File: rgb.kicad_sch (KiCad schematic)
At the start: 4 parts, among them J3 rgb, U3 TPS22916BYFPT

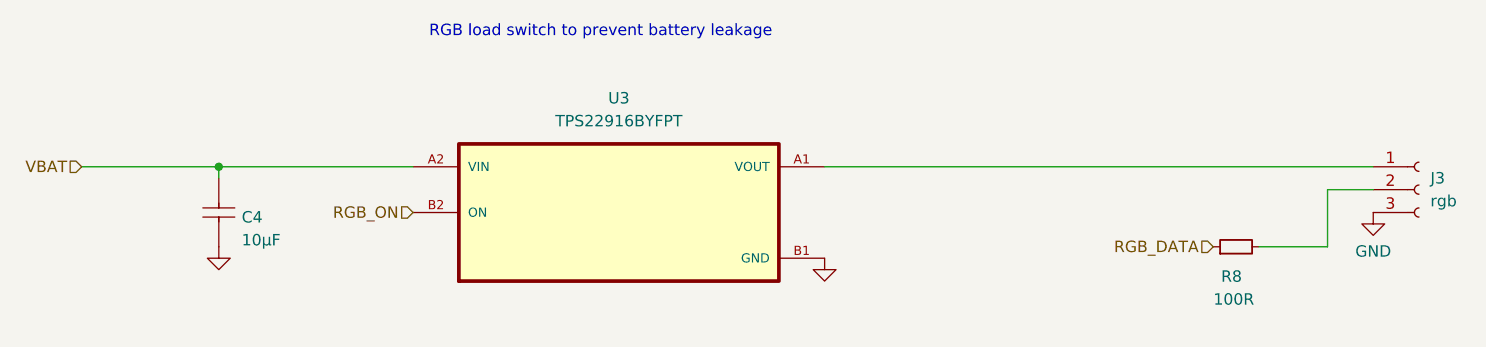
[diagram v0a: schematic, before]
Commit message: Swapping the load switches from WLSP to WSON-6 packages
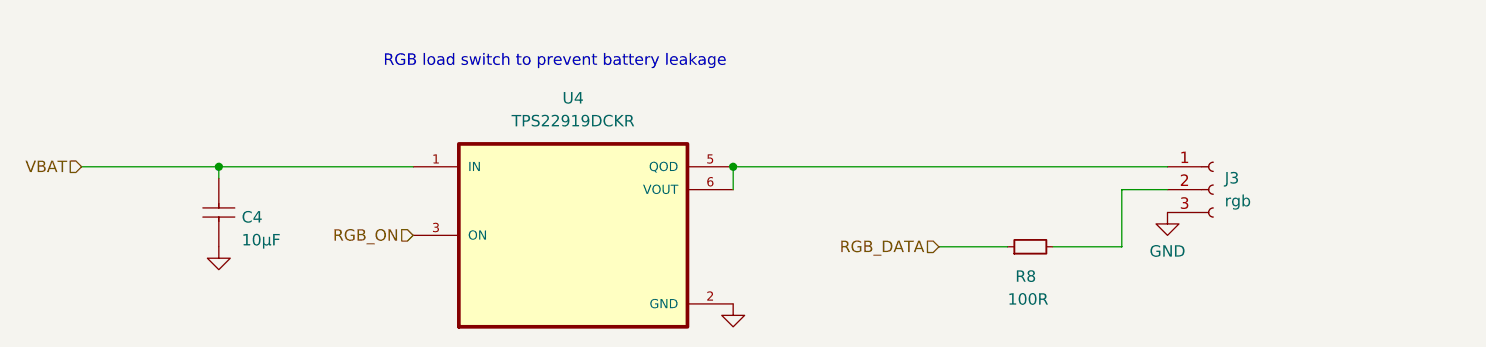
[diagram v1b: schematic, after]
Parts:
- removed U3: TPS22916BYFPT, TPS22916 load switch:BGA4C40P2X2_77X77X50, symbol TPS22916 load switch:TPS22916BYFPT
- added U4: TPS22919DCKR, TPS22919:SOT65P210X110-6N, symbol TPS22919:TPS22919DCKR
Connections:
- net GND: now also U4.2 (GND)
- net RGB_ON: now also U4.3 (ON)
- net VBAT: now also U4.1 (IN)
- net at J3.1 (Pin_1): now also U4.5 (QOD), U4.6 (VOUT)
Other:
- moved on the sheet: J3, R8

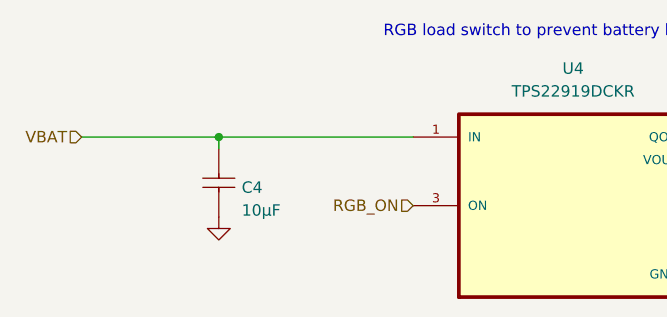
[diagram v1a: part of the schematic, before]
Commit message: Relinking the schematics and the PCB again
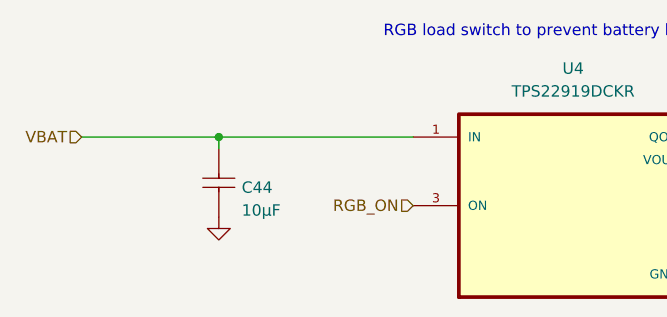
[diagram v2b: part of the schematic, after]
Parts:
- renumbered C4 to C44
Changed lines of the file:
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@@
 		(on_board yes)
 		(dnp no)
-		(property "Reference" "C4"
+		(property "Reference" "C44"
 			(at 68.58 104.14 0)
 			(effects
@@
 			(project "little-wing"
 				(path "/3a835e6f-a660-4b38-a102-87841cdd95ed/95df33f4-bbca-475a-b4f9-9e753f1a5f8c"
-					(reference "C4")
+					(reference "C44")
 					(unit 1)
 				)

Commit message: Re-linking the PCB properties back to the schematics
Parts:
- C44: footprint Passive:CAPC1608X06L -> Library:C_0603_1608
- R8: footprint Resistor_SMD:R_0201_0603Metric -> Library:R_0402_1005
- U4: footprint TPS22919:SOT65P210X110-6N -> Package_TO_SOT_SMD:SOT-363_SC-70-6
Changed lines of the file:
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@@
 			)
 		)
-		(property "Footprint" "Resistor_SMD:R_0201_0603Metric"
+		(property "Footprint" "Library:R_0402_1005"
 			(at 156.21 106.68 0)
 			(effects
@@
 			)
 		)
-		(property "Footprint" "TPS22919:SOT65P210X110-6N"
+		(property "Footprint" "Package_TO_SOT_SMD:SOT-363_SC-70-6"
 			(at 105.41 105.41 0)
 			(effects
@@
 			)
 		)
-		(property "Footprint" "Passive:CAPC1608X06L"
+		(property "Footprint" "Library:C_0603_1608"
 			(at 66.04 106.68 0)
 			(effects

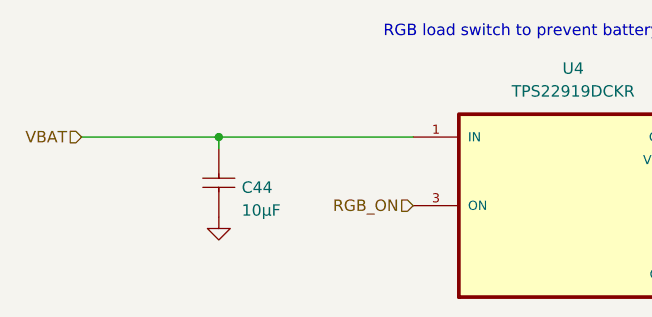
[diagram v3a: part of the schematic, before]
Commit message: Wiring up the load swiches side of the PCB
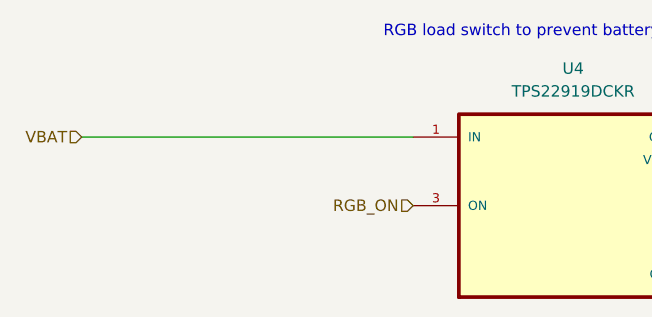
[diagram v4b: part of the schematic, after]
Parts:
- removed C44: 10µF, Library:C_0603_1608, symbol Nordic Passive DB:root_1_CAP_Nordic Passive DB.DbLib

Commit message: Further optimising the BOM and adding JLCPCB specific part numbers
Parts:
- J3: LCSC (none) -> C160403
- R8: LCSC (none) -> C25076
- U4: LCSC (none) -> C2149796
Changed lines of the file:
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@@
 			)
 		)
-		(property "LCSC" ""
+		(property "LCSC" "C25076"
 			(at 156.21 106.68 0)
+			(effects
+				(font
+					(size 1.27 1.27)
+				)
+				(hide yes)
+			)
+		)
+		(property "AVAILABILITY" ""
+			(at 156.21 106.68 90)
+			(effects
+				(font
+					(size 1.27 1.27)
+				)
+				(hide yes)
+			)
+		)
+		(property "DESCRIPTION" ""
+			(at 156.21 106.68 90)
+			(effects
+				(font
+					(size 1.27 1.27)
+				)
+				(hide yes)
+			)
+		)
+		(property "PACKAGE" ""
+			(at 156.21 106.68 90)
+			(effects
+				(font
+					(size 1.27 1.27)
+				)
+				(hide yes)
+			)
+		)
+		(property "PRICE" ""
+			(at 156.21 106.68 90)
 			(effects
 				(font
@@
 			)
 		)
+		(property "AVAILABILITY" ""
+			(at 176.53 100.33 0)
+			(effects
+				(font
+					(size 1.27 1.27)
+				)
+				(hide yes)
+			)
+		)
+		(property "DESCRIPTION" ""
+			(at 176.53 100.33 0)
+			(effects
+				(font
+					(size 1.27 1.27)
+				)
+				(hide yes)
+			)
+		)
+		(property "PACKAGE" ""
+			(at 176.53 100.33 0)
+			(effects
+				(font
+					(size 1.27 1.27)
+				)
+				(hide yes)
+			)
+		)
+		(property "PRICE" ""
+			(at 176.53 100.33 0)
+			(effects
+				(font
+					(size 1.27 1.27)
+				)
+				(hide yes)
+			)
+		)
+		(property "LCSC" "C160403"
+			(at 176.53 100.33 0)
+			(effects
+				(font
+					(size 1.27 1.27)
+				)
+				(hide yes)
+			)
+		)
 		(pin "1"
 		)
@@
 				(hide yes)
 			)
+		)
+		(property "AVAILABILITY" ""
+			(at 105.41 105.41 0)
+			(effects
+				(font
+					(size 1.27 1.27)
+				)
+				(hide yes)
+			)
+		)
+		(property "DESCRIPTION" ""
+			(at 105.41 105.41 0)
+			(effects
+				(font
+					(size 1.27 1.27)
+				)
+				(hide yes)
+			)
+		)
+		(property "PACKAGE" ""
+			(at 105.41 105.41 0)
+			(effects
+				(font
+					(size 1.27 1.27)
+				)
+				(hide yes)
+			)
+		)
+		(property "PRICE" ""
+			(at 105.41 105.41 0)
+			(effects
+				(font
+					(size 1.27 1.27)
+				)
+				(hide yes)
+			)
+		)
+		(property "LCSC" "C2149796"
+			(at 105.41 105.41 0)
+			(effects
+				(font
+					(size 1.27 1.27)
+				)
+				(hide yes)
+			)
